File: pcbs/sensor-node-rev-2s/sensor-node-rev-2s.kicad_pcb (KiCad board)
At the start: 2 copper layers, 49 x 49 mm, 60 parts, among them IC1 NPP-301A-700AT, IC2 AD8226ARMZ, J2 DEBUG_CONN, J3 SMA EDGE CONN, J4 UART_CONN, U1 STM32U031K8U6, U4 TLV9001IDCK

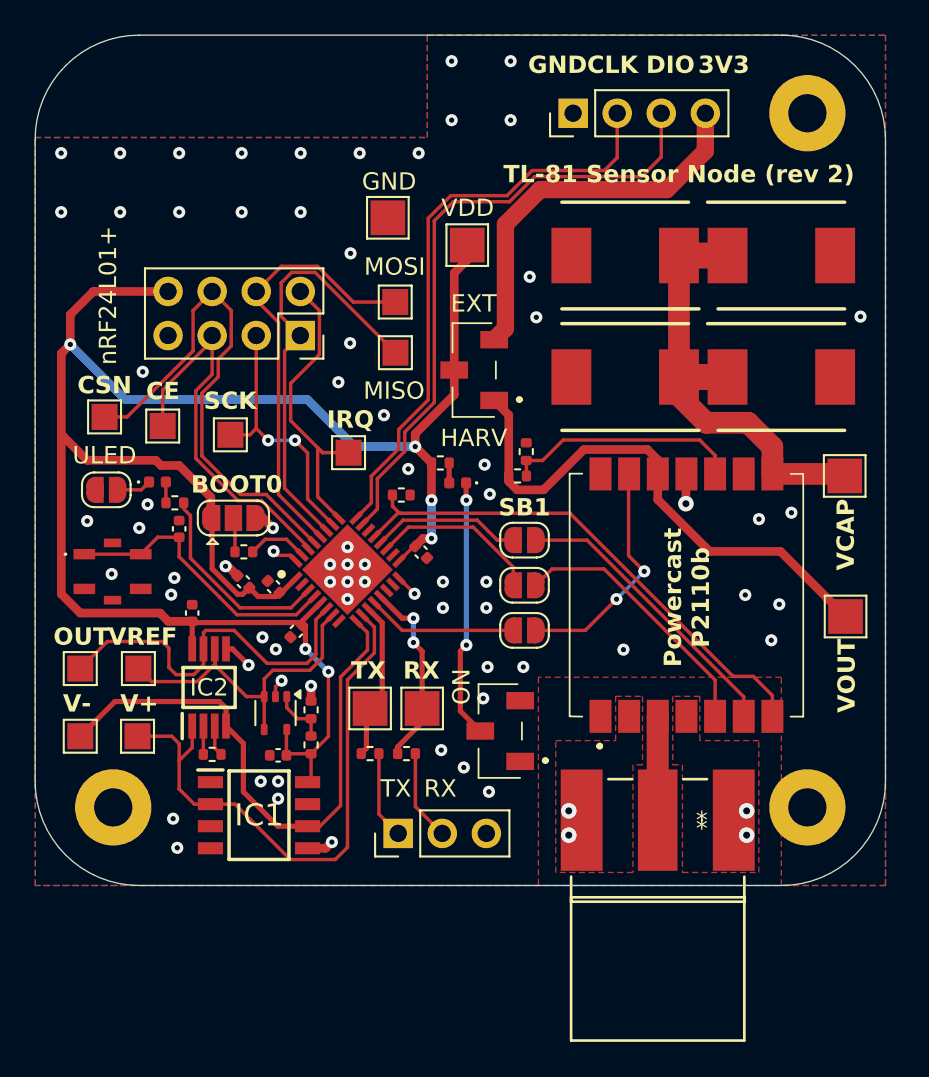
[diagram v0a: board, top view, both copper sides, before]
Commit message: Add initial manufacturing files for sensor node rev 2s
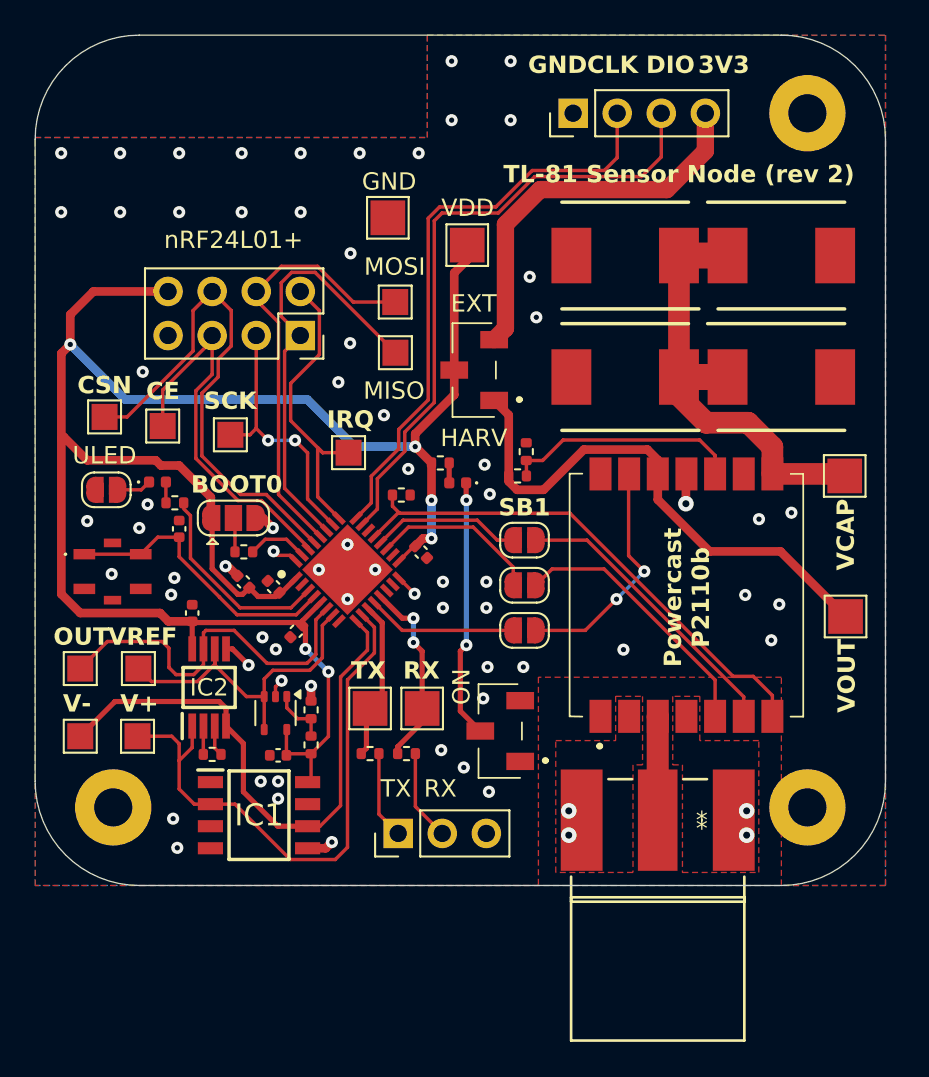
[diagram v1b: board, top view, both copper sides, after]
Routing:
- net GND: vias 77 -> 72
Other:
- board text added: "Mihir Nimgade 2024-07"

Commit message: Add little guy and update manufacturing files for rev 2s
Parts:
- added G***: LOGO, LOGO, B.Cu at (113.7, 110.0)

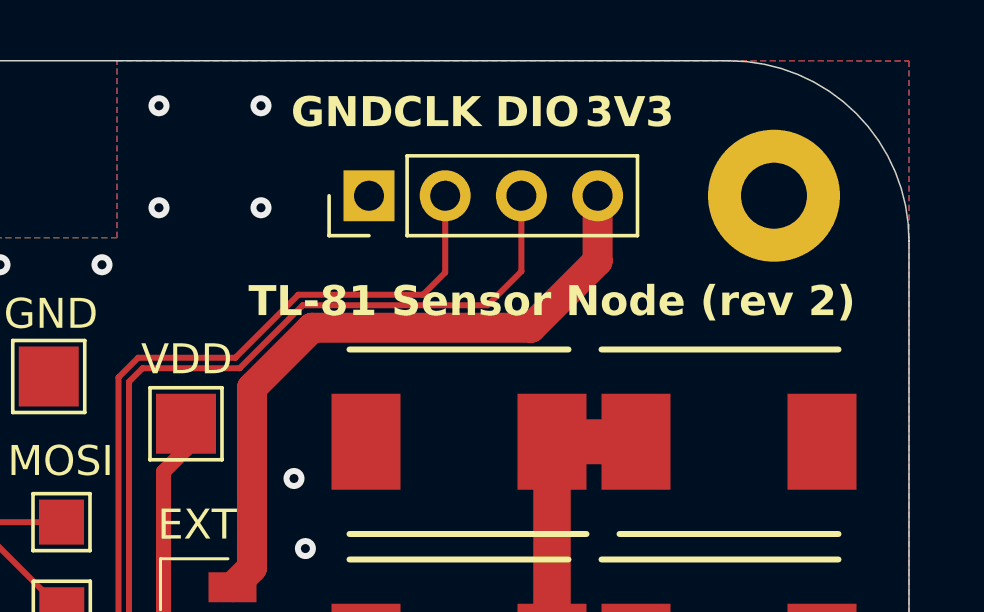
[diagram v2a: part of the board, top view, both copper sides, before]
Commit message: Update silkscreen and manu files for rev 2s
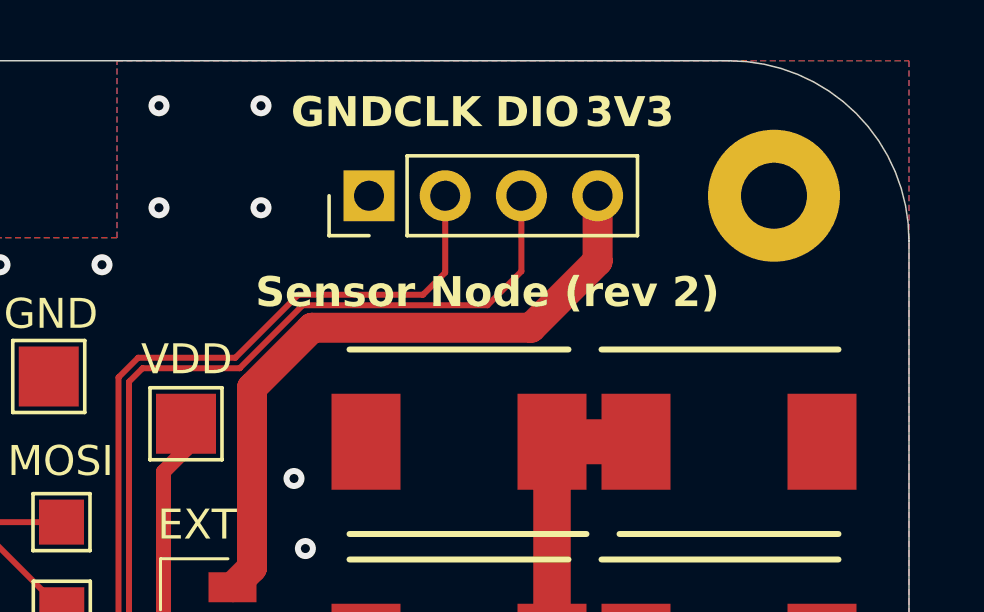
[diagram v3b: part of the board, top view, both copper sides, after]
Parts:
- moved G*** 5.14 mm to (115.9, 114.7)
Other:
- board text added: "Sensor Node (rev 2)"
- board text added: "Sensor Node Mihir Nimgade 2024-07"
- board text removed: "Mihir Nimgade 2024-07"
- board text removed: "TL-81 Sensor Node (rev 2)"
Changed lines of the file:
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@@
 	(footprint "LOGO"
 		(layer "B.Cu")
-		(at 113.7 110 180)
+		(at 115.9 114.65 180)
 		(property "Reference" "G***"
 			(at 0 0 180)
@@
 		(layer "Edge.Cuts")
 	)
-	(gr_text "Mihir Nimgade\n2024-07"
-		(at 121.5 104.5 90)
+	(gr_text "Sensor Node\nMihir Nimgade\n2024-07"
+		(at 120.65 108.7 0)
 		(layer "B.SilkS")
 		(effects
@@
 		)
 	)
-	(gr_text "TL-81 Sensor Node (rev 2)"
-		(at 111.1 104.6 0)
-		(layer "F.SilkS")
-		(effects
+	(gr_text "Sensor Node (rev 2)"
+		(at 108.95 104.3 0)
+		(layer "F.SilkS")
+		(effects
